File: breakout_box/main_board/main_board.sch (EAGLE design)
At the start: 31 parts, among them CN1 19PIN_LEMO, Q1 DMP3099L, Q2 DSS6060

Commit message: commit and push eagle files for Nexus v2.3
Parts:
- removed C7: 1nF, resistor:C-EUC0402K
- removed D1: FM4004W, CYCFI_diode:FM4007W
- removed H10, H11, H12, H13, H5: (no value), con-lstb:MA03-1_EDITED
- removed H14: MA02-1, con-lstb:MA02-1
- removed H9: (no value), con-lstb:MA08-1
- removed L1: 1mH, inductors:SDR
- removed L2: 82uH, resistor:L-EU
- added H17: (no value), con-lstb:MA08-1
- added JP1, JP10, JP11, JP12, JP13, JP2, JP3, JP4, JP5, JP6, JP7, JP8, JP9: (no value), pinhead-2:PINHD-1X03_2.00
- added R3: 12k, resistor:R-EU_R0603
- added R4: 4.7k, resistor:R-EU_R0402
- C1, C3: value 22uF -> 470uF; device resistor:C-EUC0805 -> resistor:CPOL-EU140CLH-1010
- C4: value 1uF -> 470uF; device resistor:C-EUC0603 -> resistor:CPOL-EU140CLH-1010
- C5: value 10uF -> 1uF
- C6: value 1000uF -> 0.1uF; device resistor:CPOL-EU140CLH-1010 -> resistor:C-EUC0603
- H1, H2: value (none) -> DNP
- H3, H4: device con-lstb:MA03-1_EDITED -> con-lstb:MA08-1
- H6: value (none) -> MA02-1; device con-lstb:MA08-1 -> con-lstb:MA02-1
- Q2: value DSS6060 -> TIP122; device CYCFI_semicon:DSS60601MZ4-13 -> CYCFI_semicon:TIP122
- R1: value 1k -> 220R; device resistor:R-EU_R0402 -> resistor:R-EU_R0603
- R2: value 4.7k -> 220R; device resistor:R-EU_R0402 -> resistor:R-EU_R0603
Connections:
- removed net +AVCC: C4.1, C5.1, C7.1, CN1.16, CN1.17, D1.A, H1.14, H1.15, H9.1, H9.2, Q2.E, R2.1
- removed net +DVCC: C3.1, H1.8, H1.9, H9.5, H9.6, L1.2
- removed net N$20: C2.+, Q2.B, R1.1
- new net GND1: H4.5, H4.6, H4.7, H4.8
- new net N$22: H2.15, JP9.1
- new net N$23: JP11.3, JP8.2
- new net N$31: CN1.3, H17.3, H2.3, H3.3
- new net N$39: CN1.4, H17.4, H2.4, H3.4
- new net N$40: JP12.3, JP7.2
- new net N$41: CN1.6, H17.6, H2.6, H3.6
- new net N$43: H2.8, H3.8, JP2.1
- new net N$44: JP13.3, JP6.2
- new net V_AUX: C1.+, H8.5, H8.6, JP10.1, JP11.1, Q1.S, Q2.C, R1.2
- new net V_OUT: C4.+, C5.1, C6.1, CN1.16, CN1.17, H1.12, H1.13, H1.14, H1.15, H8.1, H8.2, Q2.E, R4.1
- net GND: now also C1.-, C3.-, C4.-, C6.2, H1.8, H1.9, H6.1, H8.3, H8.4, H8.7, H8.8, JP12.1, JP13.1, R3.1; no longer C1.2, C3.2, C4.2, C6.-, C7.2, H1.12, H1.13, H14.1, H7.5, H7.6, H7.7, H7.8, H9.3, H9.4, H9.7, H9.8
- net N$1: now also CN1.2, H17.2, H2.2, H3.2; no longer H2.13, H3.1
- net N$10: now also JP10.3, JP9.2; no longer CN1.6, H2.6, H6.6
- net N$11: now also H3.7, JP1.1; no longer CN1.7, H6.7
- net N$12: now also CN1.7, JP1.2; no longer CN1.8, H2.8, H6.8
- net N$13: now also H1.1, H7.2, JP3.3; no longer CN1.9, H10.2
- net N$14: now also JP4.2; no longer H11.2
- net N$15: now also JP5.2; no longer H12.2
- net N$16: now also JP13.2; no longer H13.2
- net N$17: now also CN1.9, JP3.2; no longer H2.15, H5.1
- net N$18: now also H4.2, JP4.1; no longer H11.1, H7.2
- net N$19: now also H2.13, JP7.1; no longer C1.1, L1.1, L2.1, Q1.S
- net N$2: now also CN1.1, H17.1, H2.1, H3.1; no longer H14.2, Q1.D
- net N$21: now also H2.14, JP8.1; no longer C6.+, D1.C, L2.2, Q2.C, R1.2
- net N$25: now also R4.2; no longer R2.2
- net N$26: now also H7.4, JP5.3; no longer H12.3, H8.3
- net N$27: now also H7.3, JP4.3; no longer H11.3, H8.2
- net N$28: now also H4.4, JP6.1; no longer H13.1, H7.4
- net N$29: now also H4.3, JP5.1; no longer H12.1, H7.3
- net N$3: now also CN1.8, JP2.2; no longer H2.14, H4.1
- net N$30: now also H7.5, JP6.3; no longer H13.3, H8.4
- net N$32: now also H17.7, H4.1, JP3.1; no longer H10.1, H7.1
- net N$33: now also H7.6, JP7.3; no longer H3.3, H8.5
- net N$34: now also H7.7, JP8.3; no longer H4.3, H8.6
- net N$35: now also H7.8, JP9.3; no longer H5.3, H8.7
- net N$36: now also JP12.2; no longer H3.2
- net N$37: now also JP11.2; no longer H4.2
- net N$38: now also JP10.2; no longer H5.2
- net N$4: now also H6.2, Q1.D; no longer CN1.1, H2.1, H6.1
- net N$5: now also H7.1, JP2.3; no longer CN1.2, H2.2, H6.2
- net N$6: now also C3.+, Q2.B, R2.1, R3.2; no longer CN1.3, H2.3, H6.3
- net N$7: now also H17.8, JP1.3; no longer CN1.4, H2.4, H6.4
- net N$8: now also C2.+, R1.1, R2.2; no longer CN1.5, H2.5, H6.5
- net N$9: now also CN1.5, H17.5, H2.5, H3.5; no longer H1.1, H10.3, H8.1
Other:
- note added: "CH15_GK/CV"
- note added: "CH1_GK"
- note added: "CH2_GK"
- note added: "CH3_GK"
- note added: "CH4_GK"
- note added: "CH5_GK"
- note added: "CH6_GK"
- note added: "CH7_GK/CV"
- note added: "CH8_GK/CV"
- note added: "CV/ SW"
- note added: "Infinity"
- note added: "MONO_GK"
- note added: "Main Board"
- note added: "Main Board for Nexus Project by Cycfi Research is licensed under a Creative Commons Attribution -ShareAlike 4.0 International License. Copyright CYCFI Research Inc. 2013-2020"
- note added: "Nexus"
- note added: "To GK/MIDI Module"
- note added: "V_AUX"
- note added: "V_OUT"
- note added: "v2.3"
- note removed: "+AVCC"
- note removed: "+DVCC"
- note removed: "2016050"
- note removed: "CV"
- note removed: "Channel Distribution"
- note removed: "Main Board for Nexus Project by Cycfi Research is licensed under a Creative Commons Attribution-ShareAlike 4.0 International License. Copyright CYCFI Research Inc. 2013-2016"
- note removed: "Main Power Source"
- note removed: "NOTE: *CH9_A = Channel9 Audio *CH9_CV = Channel9 Control Voltage *NC = No Connection"
- note removed: "NOTE: *DGND = Digital Ground *AGND = Analog Ground *+12V_REG = 12V Regulated Power Supply"
- note removed: "NOTES: *+12V_REG = 12V Regulater Power Supply for Analog * +12_VREGD = 12V Regulater Power Supply for Digital *AGND = Analog Ground *DGND= Digital Ground"
- note removed: "To MIDI Module"
- note removed: "v0.96"

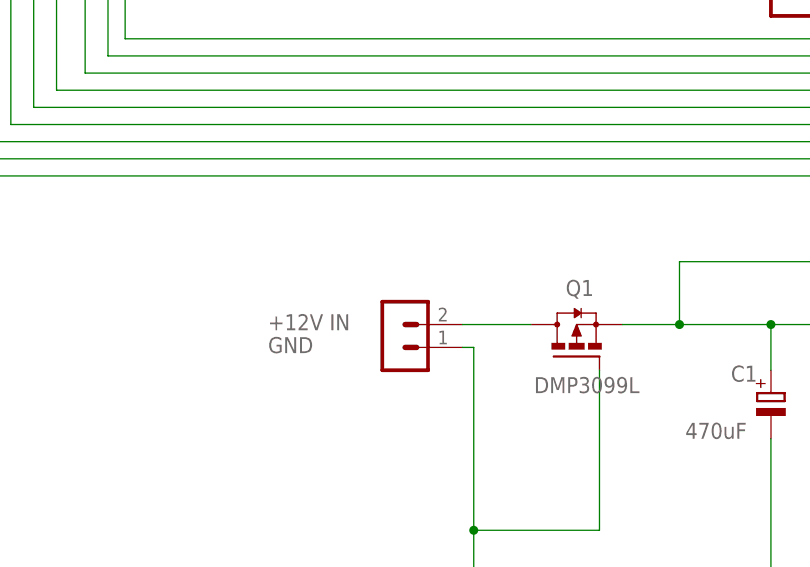
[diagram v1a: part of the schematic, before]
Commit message: update boms and pdf for shematics files
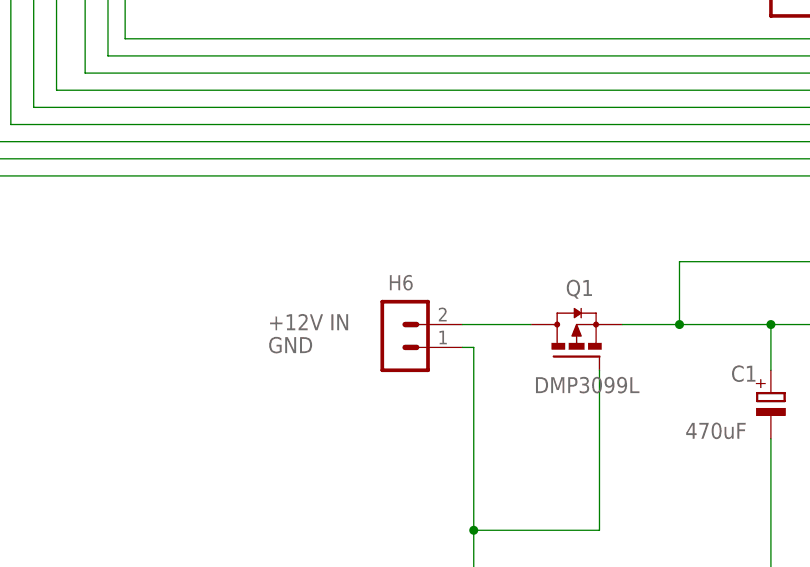
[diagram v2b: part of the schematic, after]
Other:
- note added: "H6"
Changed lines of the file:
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@@
 <rectangle x1="351.94875" y1="31.90875" x2="360.07675" y2="31.97225" layer="95"/>
 <rectangle x1="360.64825" y1="31.90875" x2="362.99775" y2="31.97225" layer="95"/>
+<text x="109.22" y="58.42" size="1.6764" layer="95">H6</text>
 </plain>
 <instances>

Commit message: Updates in Mainboard
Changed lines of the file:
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@@
 <setting verticaltext="up"/>
 </settings>
-<grid distance="0.1" unitdist="inch" unit="inch" style="lines" multiple="1" display="no" altdistance="0.01" altunitdist="inch" altunit="inch"/>
+<grid distance="0.025" unitdist="inch" unit="inch" style="lines" multiple="1" display="yes" altdistance="0.01" altunitdist="inch" altunit="inch"/>
 <layers>
 <layer number="1" name="Top" color="4" fill="1" visible="no" active="no"/>
@@
 <text x="162.56" y="105.41" size="1.778" layer="95">CV/ SW</text>
 <text x="162.56" y="90.17" size="1.778" layer="95">CV/ SW</text>
-<text x="125.73" y="151.765" size="1.778" layer="95">Nexus</text>
-<text x="125.73" y="136.525" size="1.778" layer="95">Nexus</text>
-<text x="125.73" y="121.285" size="1.778" layer="95">Nexus</text>
-<text x="125.73" y="105.41" size="1.778" layer="95">Nexus</text>
-<text x="114.935" y="151.765" size="1.778" layer="95">Infinity</text>
-<text x="116.205" y="136.525" size="1.778" layer="95">Infinity</text>
-<text x="115.57" y="121.285" size="1.778" layer="95">Infinity</text>
-<text x="115.57" y="105.41" size="1.778" layer="95">Infinity</text>
+<text x="127.635" y="140.335" size="1.778" layer="95">Nexus</text>
+<text x="129.54" y="133.985" size="1.778" layer="95">Nexus</text>
+<text x="129.54" y="118.11" size="1.778" layer="95">Nexus</text>
+<text x="129.54" y="102.235" size="1.778" layer="95">Nexus</text>
+<text x="108.585" y="149.225" size="1.778" layer="95">Infinity</text>
+<text x="108.585" y="133.985" size="1.778" layer="95">Infinity</text>
+<text x="109.22" y="118.745" size="1.778" layer="95">Infinity</text>
+<text x="109.22" y="102.87" size="1.778" layer="95">Infinity</text>
 <text x="280.67" y="88.9" size="1.778" layer="95">AGND</text>
 <text x="280.67" y="91.44" size="1.778" layer="95">AGND</text>
@@
 <instance part="H4" gate="1" x="361.315" y="219.71" rot="R180"/>
 <instance part="H17" gate="1" x="276.225" y="148.59" rot="R180"/>
-<instance part="JP1" gate="A" x="158.115" y="214.63"/>
+<instance part="JP1" gate="A" x="158.115" y="214.63" smashed="yes">
+<attribute name="NAME" x="146.05" y="217.805" size="1.778" layer="95"/>
+<attribute name="VALUE" x="151.765" y="207.01" size="1.778" layer="96"/>
+</instance>
 <instance part="JP2" gate="A" x="158.115" y="200.025"/>
 <instance part="JP3" gate="A" x="158.115" y="185.42"/>
@@
 <net name="N$28" class="0">
 <segment>
-<wire x1="155.575" y1="142.24" x2="133.35" y2="142.24" width="0.1524" layer="91"/>
-<wire x1="133.35" y1="142.24" x2="133.35" y2="229.235" width="0.1524" layer="91"/>
-<wire x1="133.35" y1="229.235" x2="312.42" y2="229.235" width="0.1524" layer="91"/>
+<wire x1="155.575" y1="142.24" x2="135.255" y2="142.24" width="0.1524" layer="91"/>
+<wire x1="135.255" y1="142.24" x2="135.255" y2="229.235" width="0.1524" layer="91"/>
+<wire x1="135.255" y1="229.235" x2="312.42" y2="229.235" width="0.1524" layer="91"/>
 <wire x1="312.42" y1="229.235" x2="342.9" y2="229.235" width="0.1524" layer="91"/>
 <pinref part="H2" gate="1" pin="12"/>
@@
 <wire x1="318.135" y1="177.165" x2="318.135" y2="236.855" width="0.1524" layer="91"/>
 <junction x="318.135" y="236.855"/>
-<wire x1="126.365" y1="219.075" x2="143.51" y2="219.075" width="0.1524" layer="91"/>
-<wire x1="143.51" y1="219.075" x2="143.51" y2="187.96" width="0.1524" layer="91"/>
-<wire x1="143.51" y1="187.96" x2="155.575" y2="187.96" width="0.1524" layer="91"/>
+<wire x1="126.365" y1="219.075" x2="145.415" y2="219.075" width="0.1524" layer="91"/>
+<wire x1="145.415" y1="219.075" x2="145.415" y2="187.96" width="0.1524" layer="91"/>
+<wire x1="145.415" y1="187.96" x2="155.575" y2="187.96" width="0.1524" layer="91"/>
 <wire x1="350.52" y1="236.855" x2="350.52" y2="227.33" width="0.1524" layer="91"/>
 <pinref part="H4" gate="1" pin="1"/>
@@
 <net name="N$19" class="0">
 <segment>
-<wire x1="155.575" y1="127" x2="135.89" y2="127" width="0.1524" layer="91"/>
-<wire x1="135.89" y1="127" x2="135.89" y2="226.695" width="0.1524" layer="91"/>
-<wire x1="135.89" y1="226.695" x2="310.515" y2="226.695" width="0.1524" layer="91"/>
+<wire x1="155.575" y1="127" x2="137.795" y2="127" width="0.1524" layer="91"/>
+<wire x1="137.795" y1="127" x2="137.795" y2="226.695" width="0.1524" layer="91"/>
+<wire x1="137.795" y1="226.695" x2="310.515" y2="226.695" width="0.1524" layer="91"/>
 <wire x1="310.515" y1="226.695" x2="310.515" y2="167.005" width="0.1524" layer="91"/>
 <pinref part="H2" gate="1" pin="13"/>
@@
 <net name="N$21" class="0">
 <segment>
-<wire x1="155.575" y1="111.76" x2="138.43" y2="111.76" width="0.1524" layer="91"/>
-<wire x1="138.43" y1="111.76" x2="138.43" y2="224.155" width="0.1524" layer="91"/>
-<wire x1="138.43" y1="224.155" x2="308.61" y2="224.155" width="0.1524" layer="91"/>
+<wire x1="155.575" y1="111.76" x2="140.335" y2="111.76" width="0.1524" layer="91"/>
+<wire x1="140.335" y1="111.76" x2="140.335" y2="224.155" width="0.1524" layer="91"/>
+<wire x1="140.335" y1="224.155" x2="308.61" y2="224.155" width="0.1524" layer="91"/>
 <wire x1="308.61" y1="224.155" x2="308.61" y2="164.465" width="0.1524" layer="91"/>
 <pinref part="H2" gate="1" pin="14"/>
@@
 <net name="N$22" class="0">
 <segment>
-<wire x1="155.575" y1="96.52" x2="140.97" y2="96.52" width="0.1524" layer="91"/>
-<wire x1="140.97" y1="96.52" x2="140.97" y2="221.615" width="0.1524" layer="91"/>
-<wire x1="140.97" y1="221.615" x2="306.705" y2="221.615" width="0.1524" layer="91"/>
+<wire x1="155.575" y1="96.52" x2="142.875" y2="96.52" width="0.1524" layer="91"/>
+<wire x1="142.875" y1="96.52" x2="142.875" y2="221.615" width="0.1524" layer="91"/>
+<wire x1="142.875" y1="221.615" x2="306.705" y2="221.615" width="0.1524" layer="91"/>
 <wire x1="306.705" y1="221.615" x2="306.705" y2="161.925" width="0.1524" layer="91"/>
 <pinref part="H2" gate="1" pin="15"/>

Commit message: updates
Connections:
- removed net GND1: H4.5, H4.6, H4.7, H4.8
- net GND: now also H1.20, H4.5, H4.6, H4.7, H4.8
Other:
- note added: "v2.5"
- note removed: "NC"
- note removed: "v2.3"
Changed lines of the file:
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@@
 <text x="214.757" y="164.084" size="1.778" layer="125">V_OUT</text>
 <text x="214.757" y="161.544" size="1.778" layer="125">V_OUT</text>
-<text x="218.821" y="148.844" size="1.778" layer="95">NC</text>
 <text x="214.63" y="158.75" size="1.778" layer="95">AGND</text>
 <text x="214.63" y="156.21" size="1.778" layer="95">AGND</text>
@@
 <wire x1="313.69" y1="62.23" x2="311.15" y2="64.77" width="0.1524" layer="94"/>
 <wire x1="311.15" y1="64.77" x2="295.91" y2="64.77" width="0.1524" layer="94"/>
-<text x="391.16" y="7.62" size="2.54" layer="95" font="vector">v2.3</text>
+<text x="391.16" y="7.62" size="2.54" layer="95" font="vector">v2.5</text>
 <text x="339.09" y="17.145" size="2.54" layer="95" font="vector">Main Board</text>
 <text x="363.855" y="257.175" size="1.778" layer="95">CH1</text>
@@
 <rectangle x1="360.64825" y1="31.90875" x2="362.99775" y2="31.97225" layer="95"/>
 <text x="109.22" y="58.42" size="1.6764" layer="95">H6</text>
+<text x="214.63" y="148.59" size="1.778" layer="95">AGND</text>
 </plain>
 <instances>
@@
 <instance part="H17" gate="1" x="276.225" y="148.59" rot="R180"/>
 <instance part="JP1" gate="A" x="158.115" y="214.63" smashed="yes">
-<attribute name="NAME" x="146.05" y="217.805" size="1.778" layer="95"/>
+<attribute name="NAME" x="146.685" y="217.805" size="1.778" layer="95"/>
 <attribute name="VALUE" x="151.765" y="207.01" size="1.778" layer="96"/>
 </instance>
@@
 <wire x1="231.775" y1="157.48" x2="231.775" y2="160.02" width="0.1524" layer="91"/>
 <junction x="231.775" y="157.48"/>
+<pinref part="H1" gate="1" pin="20"/>
+<wire x1="231.775" y1="152.4" x2="231.775" y2="149.86" width="0.1524" layer="91"/>
+<junction x="231.775" y="152.4"/>
 </segment>
 <segment>
@@
 <junction x="231.775" y="175.26"/>
 </segment>
+<segment>
+<pinref part="H4" gate="1" pin="5"/>
+<wire x1="353.695" y1="217.17" x2="351.79" y2="217.17" width="0.1524" layer="91"/>
+<wire x1="351.79" y1="217.17" x2="351.79" y2="214.63" width="0.1524" layer="91"/>
+<pinref part="H4" gate="1" pin="6"/>
+<wire x1="351.79" y1="214.63" x2="353.695" y2="214.63" width="0.1524" layer="91"/>
+<wire x1="351.79" y1="214.63" x2="351.79" y2="212.09" width="0.1524" layer="91"/>
+<junction x="351.79" y="214.63"/>
+<pinref part="H4" gate="1" pin="7"/>
+<wire x1="351.79" y1="212.09" x2="353.695" y2="212.09" width="0.1524" layer="91"/>
+<wire x1="351.79" y1="212.09" x2="351.79" y2="209.55" width="0.1524" layer="91"/>
+<junction x="351.79" y="212.09"/>
+<pinref part="H4" gate="1" pin="8"/>
+<wire x1="351.79" y1="209.55" x2="353.695" y2="209.55" width="0.1524" layer="91"/>
+</segment>
 </net>
 <net name="N$14" class="0">
@@
 </segment>
 </net>
-<net name="GND1" class="0">
-<segment>
-<pinref part="H4" gate="1" pin="5"/>
-<wire x1="353.695" y1="217.17" x2="351.79" y2="217.17" width="0.1524" layer="91"/>
-<wire x1="351.79" y1="217.17" x2="351.79" y2="214.63" width="0.1524" layer="91"/>
-<pinref part="H4" gate="1" pin="6"/>
-<wire x1="351.79" y1="214.63" x2="353.695" y2="214.63" width="0.1524" layer="91"/>
-<wire x1="351.79" y1="214.63" x2="351.79" y2="212.09" width="0.1524" layer="91"/>
-<junction x="351.79" y="214.63"/>
-<pinref part="H4" gate="1" pin="7"/>
-<wire x1="351.79" y1="212.09" x2="353.695" y2="212.09" width="0.1524" layer="91"/>
-<wire x1="351.79" y1="212.09" x2="351.79" y2="209.55" width="0.1524" layer="91"/>
-<junction x="351.79" y="212.09"/>
-<pinref part="H4" gate="1" pin="8"/>
-<wire x1="351.79" y1="209.55" x2="353.695" y2="209.55" width="0.1524" layer="91"/>
-</segment>
-</net>
